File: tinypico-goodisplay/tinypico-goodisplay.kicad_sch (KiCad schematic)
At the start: 21 parts, among them Q1 Si1308, U1 TinypicoESP32_Symbol, U2 FPCConn

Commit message: Update schematic
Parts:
- added JP1: selector, symbol Jumper:Jumper_3_Bridged12
- added R3: 3R, symbol Device:R
- U1: footprint (none) -> Tinypico:TinyESP32
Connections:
- net GND: now also R3.2
- net at Q1.2 (S), U2.22 (3): now also JP1.2 (C); no longer R2.1
- new net: JP1.1 (A), R2.1
- new net: JP1.3 (B), R3.1
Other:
- company: (none) -> FASANI CORPORATION
- title: (none) -> Tinypico Goodisplay HAT
- moved on the sheet: C7, C9, R1

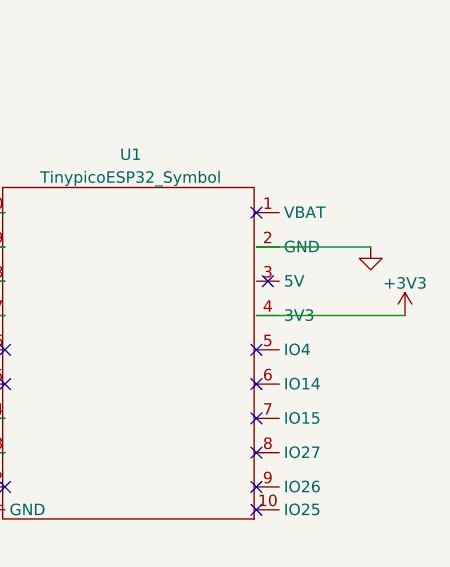
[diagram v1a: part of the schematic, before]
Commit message: Update netlist and schematic
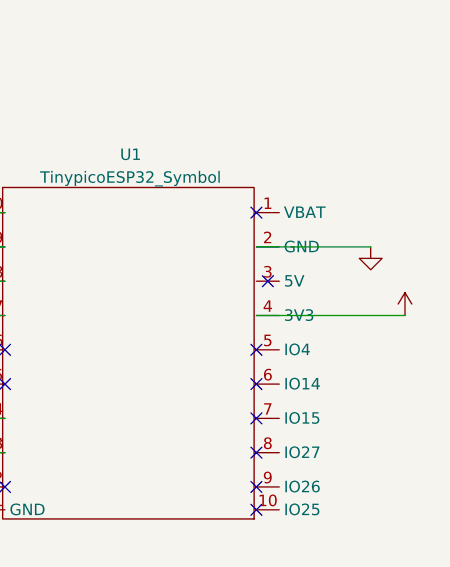
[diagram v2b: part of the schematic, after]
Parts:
- U2: footprint Connector_FFC-FPC:TE_2-1734839-4_1x24-1MP_P0.5mm_Horizontal -> (none)
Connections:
- net +3.3VP: now also U1.4 (3V3)
- net +3V3: no longer U1.4 (3V3)
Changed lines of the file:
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@@
       (effects (font (size 1.27 1.27)) (justify right))
     )
-    (property "Footprint" "Connector_FFC-FPC:TE_2-1734839-4_1x24-1MP_P0.5mm_Horizontal" (id 2) (at 58.42 153.67 0)
+    (property "Footprint" "" (id 2) (at 58.42 153.67 0)
       (effects (font (size 1.27 1.27)) hide)
     )
@@
     (pin "3")
   )
-  (symbol (lib_id "power:+3V3") (at 243.84 91.44 0) (unit 1)
-    (in_bom yes) (on_board yes) (fields_autoplaced)
-    (property "Reference" "#PWR0103" (id 0) (at 243.84 95.25 0)
-      (effects (font (size 1.27 1.27)) hide)
-    )
-    (property "Value" "+3V3" (id 1) (at 243.84 87.8642 0))
-    (property "Footprint" "" (id 2) (at 243.84 91.44 0)
-      (effects (font (size 1.27 1.27)) hide)
-    )
-    (property "Datasheet" "" (id 3) (at 243.84 91.44 0)
-      (effects (font (size 1.27 1.27)) hide)
-    )
-    (pin "1")
-  )
   (symbol (lib_id "power:GND") (at 110.49 158.75 0) (unit 1)
     (in_bom yes) (on_board yes)
@@
     (pin "1")
   )
+  (symbol (lib_id "power:+3.3VP") (at 243.84 91.44 0) (unit 1)
+    (in_bom yes) (on_board yes)
+    (property "Reference" "#PWR0103" (id 0) (at 247.65 92.71 0)
+      (effects (font (size 1.27 1.27)) hide)
+    )
+    (property "Value" "" (id 1) (at 244.221 87.0458 0))
+    (property "Footprint" "" (id 2) (at 243.84 91.44 0)
+      (effects (font (size 1.27 1.27)) hide)
+    )
+    (property "Datasheet" "" (id 3) (at 243.84 91.44 0)
+      (effects (font (size 1.27 1.27)) hide)
+    )
+    (pin "1")
+  )
   (symbol (lib_id "Device:R") (at 105.41 158.75 90) (unit 1)
     (in_bom yes) (on_board yes)
@@
       (reference "#PWR0102") (unit 1) (value "~") (footprint "")
     )
-    (path "/8e863a4d-74d3-41c7-b4a8-ba78ccdc5b0c"
-      (reference "#PWR0103") (unit 1) (value "+3V3") (footprint "")
+    (path "/e450b142-5c2d-4bec-b9c4-1540c3d86e20"
+      (reference "#PWR0103") (unit 1) (value "+3.3VP") (footprint "")
     )
     (path "/00000000-0000-0000-0000-0000606b9968"
@@
     )
     (path "/00000000-0000-0000-0000-00006072c514"
-      (reference "U2") (unit 1) (value "FPCConn") (footprint "Connector_FFC-FPC:TE_2-1734839-4_1x24-1MP_P0.5mm_Horizontal")
-    )
-  )
+      (reference "U2") (unit 1) (value "FPCConn") (footprint "footprint:Hirose_FH12-24S-0.5SH_1x24-1MP_P0.50mm_Horizontal")
+    )
+  )

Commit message: SCH works, dont touch
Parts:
- U2: footprint (none) -> footprint:Hirose_FH12-24S-0.5SH_1x24-1MP_P0.50mm_Horizontal
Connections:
- net +3.3VP is gone; now on net +3V3: C8.2, U1.4 (3V3), U2.10 (15), U2.9 (16)
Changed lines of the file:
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@@
   (junction (at 110.49 146.05) (diameter 0) (color 0 0 0 0)
   )
+  (junction (at 68.58 121.92) (diameter 0) (color 0 0 0 0)
+  )
   (junction (at 88.9 114.3) (diameter 0) (color 0 0 0 0)
-  )
-  (junction (at 66.04 121.92) (diameter 0) (color 0 0 0 0)
   )
   (junction (at 88.9 104.14) (diameter 0) (color 0 0 0 0)
@@
     (stroke (width 0) (type default) (color 0 0 0 0))
   )
-  (wire (pts (xy 62.23 121.92) (xy 66.04 121.92))
+  (wire (pts (xy 62.23 121.92) (xy 68.58 121.92))
     (stroke (width 0) (type default) (color 0 0 0 0))
   )
@@
     (stroke (width 0) (type default) (color 0 0 0 0))
   )
+  (wire (pts (xy 68.58 121.92) (xy 72.39 121.92))
+    (stroke (width 0) (type default) (color 0 0 0 0))
+  )
   (wire (pts (xy 86.36 101.6) (xy 88.9 101.6))
     (stroke (width 0) (type default) (color 0 0 0 0))
@@
   )
   (wire (pts (xy 77.47 114.3) (xy 80.01 114.3))
-    (stroke (width 0) (type default) (color 0 0 0 0))
-  )
-  (wire (pts (xy 72.39 121.92) (xy 66.04 121.92))
     (stroke (width 0) (type default) (color 0 0 0 0))
   )
@@
     (pin "1")
   )
-  (symbol (lib_id "power:+3.3VP") (at 66.04 121.92 0) (unit 1)
-    (in_bom yes) (on_board yes)
-    (property "Reference" "#PWR0113" (id 0) (at 69.85 123.19 0)
-      (effects (font (size 1.27 1.27)) hide)
-    )
-    (property "Value" "+3.3VP" (id 1) (at 66.421 117.5258 0))
-    (property "Footprint" "" (id 2) (at 66.04 121.92 0)
-      (effects (font (size 1.27 1.27)) hide)
-    )
-    (property "Datasheet" "" (id 3) (at 66.04 121.92 0)
-      (effects (font (size 1.27 1.27)) hide)
-    )
-    (pin "1")
-  )
   (symbol (lib_id "power:GND") (at 52.07 161.29 0) (unit 1)
     (in_bom yes) (on_board yes)
@@
       (effects (font (size 1.27 1.27)) (justify right))
     )
-    (property "Footprint" "" (id 2) (at 58.42 153.67 0)
+    (property "Footprint" "footprint:Hirose_FH12-24S-0.5SH_1x24-1MP_P0.50mm_Horizontal" (id 2) (at 58.42 153.67 0)
       (effects (font (size 1.27 1.27)) hide)
     )
@@
     (pin "3")
   )
+  (symbol (lib_id "power:+3V3") (at 243.84 91.44 0) (unit 1)
+    (in_bom yes) (on_board yes) (fields_autoplaced)
+    (property "Reference" "#PWR?" (id 0) (at 243.84 95.25 0)
+      (effects (font (size 1.27 1.27)) hide)
+    )
+    (property "Value" "" (id 1) (at 243.84 87.8642 0))
+    (property "Footprint" "" (id 2) (at 243.84 91.44 0)
+      (effects (font (size 1.27 1.27)) hide)
+    )
+    (property "Datasheet" "" (id 3) (at 243.84 91.44 0)
+      (effects (font (size 1.27 1.27)) hide)
+    )
+    (pin "1")
+  )
   (symbol (lib_id "power:GND") (at 110.49 158.75 0) (unit 1)
     (in_bom yes) (on_board yes)
@@
     )
     (property "Datasheet" "" (id 3) (at 110.49 158.75 0)
+      (effects (font (size 1.27 1.27)) hide)
+    )
+    (pin "1")
+  )
+  (symbol (lib_id "power:+3V3") (at 68.58 121.92 0) (unit 1)
+    (in_bom yes) (on_board yes) (fields_autoplaced)
+    (property "Reference" "#PWR?" (id 0) (at 68.58 125.73 0)
+      (effects (font (size 1.27 1.27)) hide)
+    )
+    (property "Value" "" (id 1) (at 68.58 118.3442 0))
+    (property "Footprint" "" (id 2) (at 68.58 121.92 0)
+      (effects (font (size 1.27 1.27)) hide)
+    )
+    (property "Datasheet" "" (id 3) (at 68.58 121.92 0)
       (effects (font (size 1.27 1.27)) hide)
     )
@@
     (pin "1")
   )
-  (symbol (lib_id "power:+3.3VP") (at 243.84 91.44 0) (unit 1)
-    (in_bom yes) (on_board yes)
-    (property "Reference" "#PWR0103" (id 0) (at 247.65 92.71 0)
-      (effects (font (size 1.27 1.27)) hide)
-    )
-    (property "Value" "" (id 1) (at 244.221 87.0458 0))
-    (property "Footprint" "" (id 2) (at 243.84 91.44 0)
-      (effects (font (size 1.27 1.27)) hide)
-    )
-    (property "Datasheet" "" (id 3) (at 243.84 91.44 0)
-      (effects (font (size 1.27 1.27)) hide)
-    )
-    (pin "1")
-  )
   (symbol (lib_id "Device:R") (at 105.41 158.75 90) (unit 1)
     (in_bom yes) (on_board yes)
@@
       (reference "#PWR0102") (unit 1) (value "~") (footprint "")
     )
-    (path "/e450b142-5c2d-4bec-b9c4-1540c3d86e20"
-      (reference "#PWR0103") (unit 1) (value "+3.3VP") (footprint "")
-    )
     (path "/00000000-0000-0000-0000-0000606b9968"
       (reference "#PWR0109") (unit 1) (value "GND") (footprint "")
@@
       (reference "#PWR0112") (unit 1) (value "GND") (footprint "")
     )
-    (path "/00000000-0000-0000-0000-0000606bdb44"
-      (reference "#PWR0113") (unit 1) (value "+3.3VP") (footprint "")
-    )
     (path "/00000000-0000-0000-0000-0000606d480f"
       (reference "#PWR0115") (unit 1) (value "GND") (footprint "")
@@
       (reference "#PWR0119") (unit 1) (value "+3V3") (footprint "")
     )
+    (path "/5c7197a8-00ce-4670-81cf-d7a0f9d1ac8c"
+      (reference "#PWR?") (unit 1) (value "+3V3") (footprint "")
+    )
+    (path "/a375fec6-08d0-4dfb-8c0d-f1c802bcfd9d"
+      (reference "#PWR?") (unit 1) (value "+3V3") (footprint "")
+    )
     (path "/00000000-0000-0000-0000-0000606b31f4"

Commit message: Update Silk
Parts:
- JP1: value selector -> (none)
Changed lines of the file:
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@@
       (effects (font (size 1.27 1.27)) (justify left))
     )
-    (property "Value" "selector" (id 1) (at 86.7162 154.1022 90)
+    (property "Value" "" (id 1) (at 86.7162 154.1022 90)
       (effects (font (size 1.27 1.27)) (justify left))
     )
@@
   (symbol (lib_id "power:+3V3") (at 243.84 91.44 0) (unit 1)
     (in_bom yes) (on_board yes) (fields_autoplaced)
-    (property "Reference" "#PWR?" (id 0) (at 243.84 95.25 0)
-      (effects (font (size 1.27 1.27)) hide)
-    )
-    (property "Value" "" (id 1) (at 243.84 87.8642 0))
+    (property "Reference" "#PWR0103" (id 0) (at 243.84 95.25 0)
+      (effects (font (size 1.27 1.27)) hide)
+    )
+    (property "Value" "+3V3" (id 1) (at 243.84 87.8642 0))
     (property "Footprint" "" (id 2) (at 243.84 91.44 0)
       (effects (font (size 1.27 1.27)) hide)
@@
   (symbol (lib_id "power:+3V3") (at 68.58 121.92 0) (unit 1)
     (in_bom yes) (on_board yes) (fields_autoplaced)
-    (property "Reference" "#PWR?" (id 0) (at 68.58 125.73 0)
-      (effects (font (size 1.27 1.27)) hide)
-    )
-    (property "Value" "" (id 1) (at 68.58 118.3442 0))
+    (property "Reference" "#PWR0104" (id 0) (at 68.58 125.73 0)
+      (effects (font (size 1.27 1.27)) hide)
+    )
+    (property "Value" "+3V3" (id 1) (at 68.58 118.3442 0))
     (property "Footprint" "" (id 2) (at 68.58 121.92 0)
       (effects (font (size 1.27 1.27)) hide)
@@
       (reference "#PWR0102") (unit 1) (value "~") (footprint "")
     )
+    (path "/5c7197a8-00ce-4670-81cf-d7a0f9d1ac8c"
+      (reference "#PWR0103") (unit 1) (value "+3V3") (footprint "")
+    )
+    (path "/a375fec6-08d0-4dfb-8c0d-f1c802bcfd9d"
+      (reference "#PWR0104") (unit 1) (value "+3V3") (footprint "")
+    )
     (path "/00000000-0000-0000-0000-0000606b9968"
       (reference "#PWR0109") (unit 1) (value "GND") (footprint "")
@@
       (reference "#PWR0119") (unit 1) (value "+3V3") (footprint "")
     )
-    (path "/5c7197a8-00ce-4670-81cf-d7a0f9d1ac8c"
-      (reference "#PWR?") (unit 1) (value "+3V3") (footprint "")
-    )
-    (path "/a375fec6-08d0-4dfb-8c0d-f1c802bcfd9d"
-      (reference "#PWR?") (unit 1) (value "+3V3") (footprint "")
-    )
     (path "/00000000-0000-0000-0000-0000606b31f4"
       (reference "C1") (unit 1) (value "105") (footprint "Capacitor_SMD:C_0805_2012Metric_Pad1.18x1.45mm_HandSolder")
@@
     )
     (path "/3a6b8f9d-0005-44a5-95a4-3e58bdf1c3ef"
-      (reference "JP1") (unit 1) (value "selector") (footprint "")
+      (reference "JP1") (unit 1) (value "selector") (footprint "Jumper:SolderJumper-3_P1.3mm_Open_Pad1.0x1.5mm")
     )
     (path "/00000000-0000-0000-0000-0000606b755b"

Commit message: Add LCSC part Nr
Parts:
- C1, C11, C2, C3, C4, C5, C6, C7, C9: LCSC (none) -> C28323
- C10, C12: LCSC (none) -> C13967
- C8: LCSC (none) -> C49678
- D1, D2, D3: LCSC (none) -> C77336
- JP1: value (none) -> selector; footprint (none) -> Jumper:SolderJumper-3_P1.3mm_Open_Pad1.0x1.5mm
- Q1: LCSC (none) -> C469327
- R1: LCSC (none) -> C17402
- R2: LCSC (none) -> C247097
- R3: LCSC (none) -> C247015
- U2: value FPCConn -> (none); footprint footprint:Hirose_FH12-24S-0.5SH_1x24-1MP_P0.50mm_Horizontal -> (none); LCSC (none) -> C202112
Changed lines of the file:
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@@
+      (effects (font (size 1.27 1.27)) hide)
+    )
+    (property "LCSC" "C77336" (id 4) (at 73.66 72.39 0)
       (effects (font (size 1.27 1.27)) hide)
     )
@@
       (effects (font (size 1.27 1.27)) hide)
     )
+    (property "LCSC" "C77336" (id 4) (at 73.66 80.01 0)
+      (effects (font (size 1.27 1.27)) hide)
+    )
     (pin "1")
     (pin "2")
@@
       (effects (font (size 1.27 1.27)) hide)
     )
+    (property "LCSC" "C77336" (id 4) (at 73.66 87.63 0)
+      (effects (font (size 1.27 1.27)) hide)
+    )
     (pin "1")
     (pin "2")
@@
     (property "Datasheet" "https://www.onsemi.com/pub/Collateral/NDS7002A-D.PDF" (id 3) (at 128.27 110.49 0)
       (effects (font (size 1.27 1.27)) (justify left) hide)
+    )
+    (property "LCSC" "C469327" (id 4) (at 128.27 110.49 0)
+      (effects (font (size 1.27 1.27)) hide)
     )
     (pin "1")
@@
       (effects (font (size 1.27 1.27)) hide)
     )
+    (property "LCSC" "C28323" (id 4) (at 73.66 99.06 90)
+      (effects (font (size 1.27 1.27)) hide)
+    )
     (pin "1")
     (pin "2")
@@
       (effects (font (size 1.27 1.27)) hide)
     )
+    (property "LCSC" "C28323" (id 4) (at 82.55 101.6 90)
+      (effects (font (size 1.27 1.27)) hide)
+    )
     (pin "1")
     (pin "2")
@@
       (effects (font (size 1.27 1.27)) hide)
     )
+    (property "LCSC" "C28323" (id 4) (at 73.66 104.14 90)
+      (effects (font (size 1.27 1.27)) hide)
+    )
     (pin "1")
     (pin "2")
@@
       (effects (font (size 1.27 1.27)) hide)
     )
+    (property "LCSC" "C28323" (id 4) (at 82.55 106.68 90)
+      (effects (font (size 1.27 1.27)) hide)
+    )
     (pin "1")
     (pin "2")
@@
       (effects (font (size 1.27 1.27)) hide)
     )
+    (property "LCSC" "C28323" (id 4) (at 73.66 109.22 90)
+      (effects (font (size 1.27 1.27)) hide)
+    )
     (pin "1")
     (pin "2")
@@
       (effects (font (size 1.27 1.27)) hide)
     )
+    (property "LCSC" "C28323" (id 4) (at 82.55 111.76 90)
+      (effects (font (size 1.27 1.27)) hide)
+    )
     (pin "1")
     (pin "2")
@@
       (effects (font (size 1.27 1.27)) hide)
     )
+    (property "LCSC" "C28323" (id 4) (at 73.66 114.3 90)
+      (effects (font (size 1.27 1.27)) hide)
+    )
     (pin "1")
     (pin "2")
@@
       (effects (font (size 1.27 1.27)) hide)
     )
+    (property "LCSC" "C49678" (id 4) (at 76.2 121.92 90)
+      (effects (font (size 1.27 1.27)) hide)
+    )
     (pin "1")
     (pin "2")
@@
       (effects (font (size 1.27 1.27)) hide)
     )
+    (property "LCSC" "C28323" (id 4) (at 73.66 143.51 90)
+      (effects (font (size 1.27 1.27)) hide)
+    )
     (pin "1")
     (pin "2")
@@
       (effects (font (size 1.27 1.27)) hide)
     )
+    (property "LCSC" "C28323" (id 4) (at 68.58 147.32 90)
+      (effects (font (size 1.27 1.27)) hide)
+    )
     (pin "1")
     (pin "2")
@@
       (effects (font (size 1.27 1.27)) hide)
     )
+    (property "LCSC" "C17402" (id 4) (at 73.66 160.02 90)
+      (effects (font (size 1.27 1.27)) hide)
+    )
     (pin "1")
     (pin "2")
@@
       (effects (font (size 1.27 1.27)) hide)
     )
+    (property "LCSC" "C13967" (id 4) (at 82.55 83.82 0)
+      (effects (font (size 1.27 1.27)) hide)
+    )
     (pin "1")
     (pin "2")
@@
       (effects (font (size 1.27 1.27)) hide)
     )
-    (property "Datasheet" "~" (id 3) (at 119.38 91.44 0)
+    (property "Datasheet" "https://datasheet.lcsc.com/lcsc/1810251812_Samsung-Electro-Mechanics-CL21B474KBFNNNE_C13967.pdf" (id 3) (at 119.38 91.44 0)
+      (effects (font (size 1.27 1.27)) hide)
+    )
+    (property "LCSC" "C13967" (id 4) (at 119.38 91.44 0)
       (effects (font (size 1.27 1.27)) hide)
     )
@@
       (effects (font (size 1.27 1.27)) (justify right))
     )
-    (property "Value" "FPCConn" (id 1) (at 45.0342 129.413 0)
+    (property "Value" "" (id 1) (at 45.0342 129.413 0)
       (effects (font (size 1.27 1.27)) (justify right))
     )
-    (property "Footprint" "footprint:Hirose_FH12-24S-0.5SH_1x24-1MP_P0.50mm_Horizontal" (id 2) (at 58.42 153.67 0)
+    (property "Footprint" "" (id 2) (at 58.42 153.67 0)
       (effects (font (size 1.27 1.27)) hide)
     )
     (property "Datasheet" "" (id 3) (at 58.42 153.67 0)
+      (effects (font (size 1.27 1.27)) hide)
+    )
+    (property "LCSC" "C202112" (id 4) (at 58.42 153.67 0)
       (effects (font (size 1.27 1.27)) hide)
     )
@@
       (effects (font (size 1.27 1.27)) (justify left))
     )
-    (property "Value" "" (id 1) (at 86.7162 154.1022 90)
+    (property "Value" "selector" (id 1) (at 86.7162 154.1022 90)
       (effects (font (size 1.27 1.27)) (justify left))
     )
-    (property "Footprint" "" (id 2) (at 85.09 152.4 0)
+    (property "Footprint" "Jumper:SolderJumper-3_P1.3mm_Open_Pad1.0x1.5mm" (id 2) (at 85.09 152.4 0)
       (effects (font (size 1.27 1.27)) hide)
     )
@@
       (effects (font (size 1.27 1.27)) hide)
     )
+    (property "LCSC" "C247097" (id 4) (at 105.41 146.05 90)
+      (effects (font (size 1.27 1.27)) hide)
+    )
     (pin "1")
     (pin "2")
@@
       (effects (font (size 1.27 1.27)) hide)
     )
+    (property "LCSC" "C247015" (id 4) (at 105.41 158.75 90)
+      (effects (font (size 1.27 1.27)) hide)
+    )
